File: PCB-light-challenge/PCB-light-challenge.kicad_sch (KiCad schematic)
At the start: 0 parts

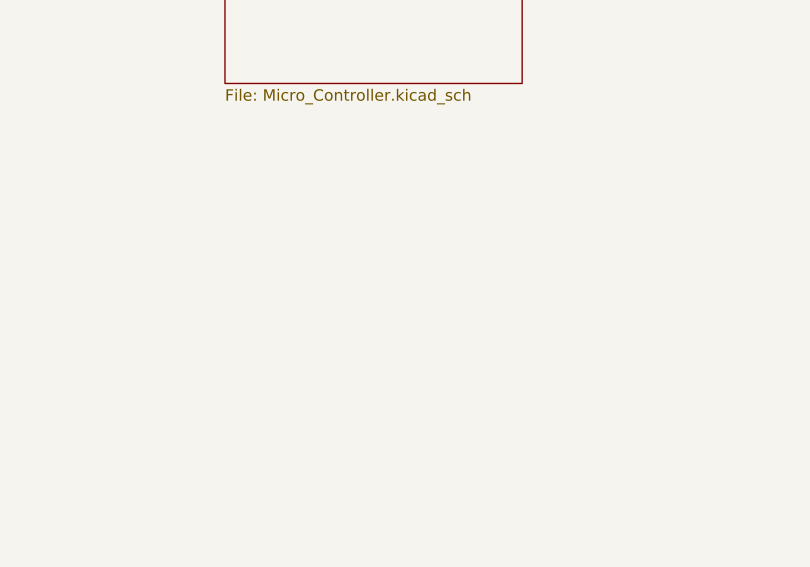
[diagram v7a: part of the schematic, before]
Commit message: schock sensor toegevoegd footprit plus symbol
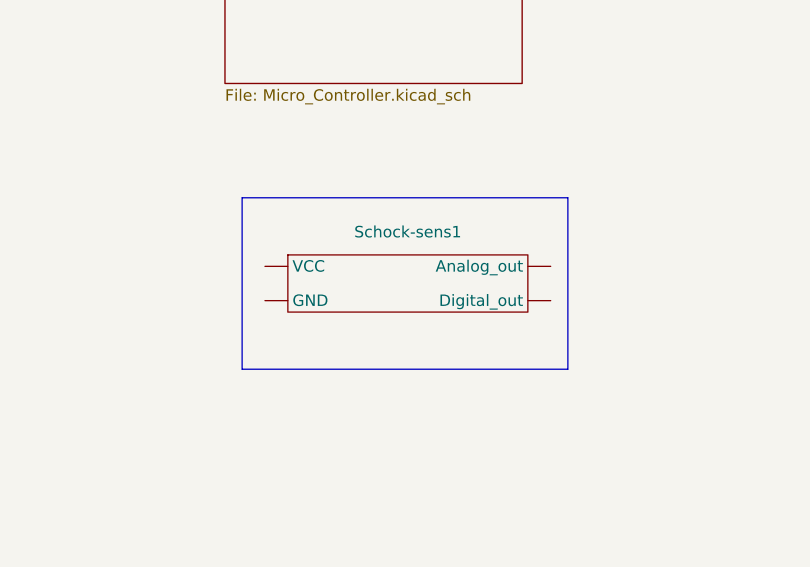
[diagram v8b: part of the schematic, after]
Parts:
- added Schock-sens1: ~, symbol Light_challenge:Schock-sens
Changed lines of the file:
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@@
 (kicad_sch (version 20230121) (generator eeschema)
   (paper "A4")
+  (rectangle (start 123.825 127) (end 160.02 146.05)
+    (stroke (width 0) (type default))
+    (fill (type none))
+  )
+  (symbol (lib_id "Light_challenge:Schock-sens") (at 141.605 132.08 0) (unit 1)
+    (in_bom yes) (on_board yes) (dnp no) (fields_autoplaced)
+    (property "Reference" "Schock-sens1" (at 142.24 130.81 0)
+      (effects (font (size 1.27 1.27)))
+    )
+    (property "Value" "~" (at 141.605 132.08 0)
+      (effects (font (size 1.27 1.27)))
+    )
+    (property "Footprint" "" (at 141.605 132.08 0)
+      (effects (font (size 1.27 1.27)) hide)
+    )
+    (property "Datasheet" "" (at 141.605 132.08 0)
+      (effects (font (size 1.27 1.27)) hide)
+    )
+    (pin "")
+    (pin "")
+    (pin "")
+    (pin "")
+    (instances
+      (project "PCB-light-challenge"
+        (path "/35573e8f-7834-430c-81d2-239f316c7834"
+          (reference "Schock-sens1") (unit 1)
+        )
+      )
+    )
+  )
   (sheet (at 38.1 25.4) (size 38.1 34.29) (fields_autoplaced)
     (stroke (width 0.1524) (type solid))
